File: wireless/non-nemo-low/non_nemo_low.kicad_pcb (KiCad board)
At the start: 2 copper layers, 260.1 x 100.6 mm, 96 parts, among them J1 Conn_01x02, J2 Conn_01x02, J3 Conn_BAT, J4 Conn_BAT, X1 5.5mm, X10 5.5mm, X2 5.5mm, X3 5.5mm, X4 5.5mm, X5 5.5mm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

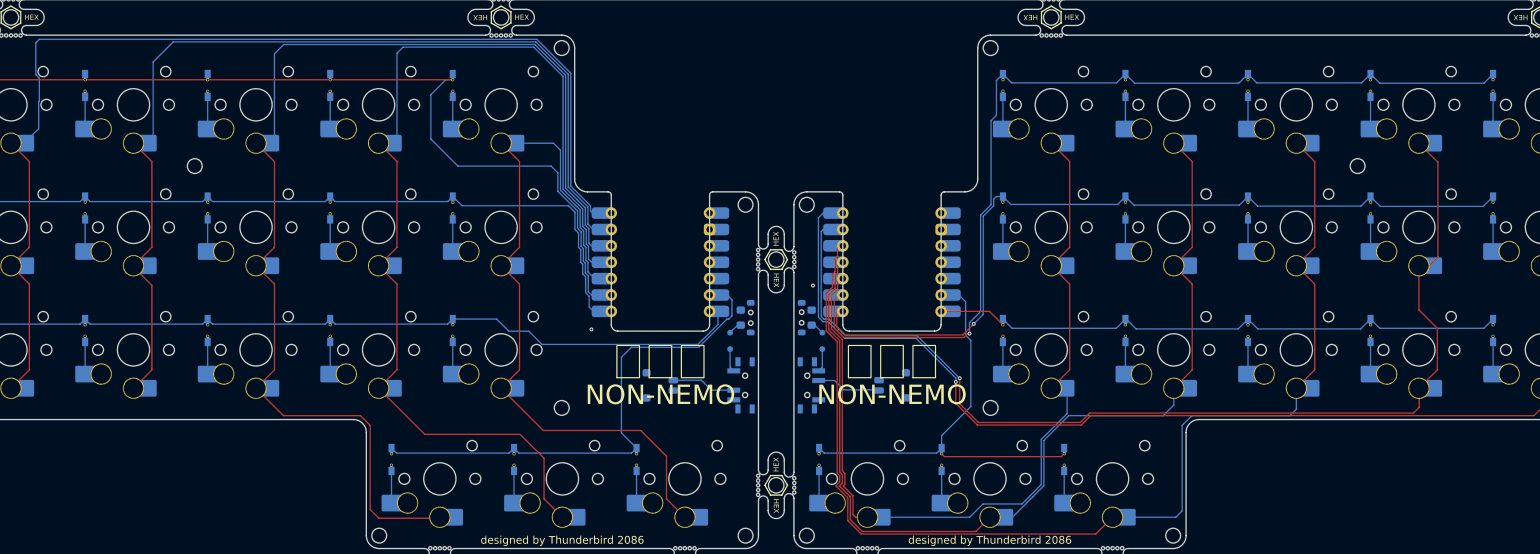
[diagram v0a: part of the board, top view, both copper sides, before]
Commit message: fixed Wired (#12)
* fixed Non Nemo Wired

* fixed ergogen for Wired
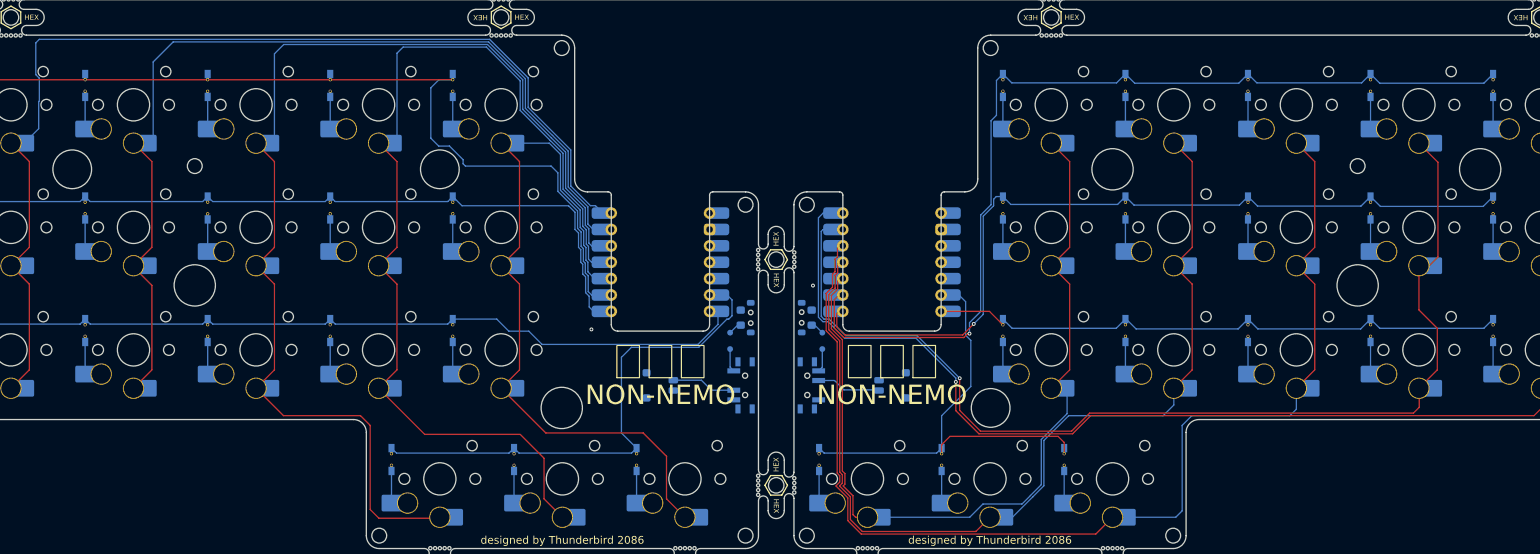
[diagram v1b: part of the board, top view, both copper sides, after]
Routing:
- net col_pinky: track 169.5 -> 164.7 mm
- net col_ring: track 150.6 -> 146.3 mm
- net col_middle: track 179.0 -> 174.7 mm
- net col_index: track 157.9 -> 153.6 mm
- net row_thumb_r: track 66.8 -> 70.6 mm
- net col_pinky_r: track 193.7 -> 195.4 mm
- net col_ring_r: track 164.9 -> 166.6 mm
- net row_top: track 131.9 -> 132.9 mm
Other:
- outline, holes or cut-outs redrawn
